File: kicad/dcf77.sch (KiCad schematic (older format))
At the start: 5 parts, among them U4 DCF77_Generic

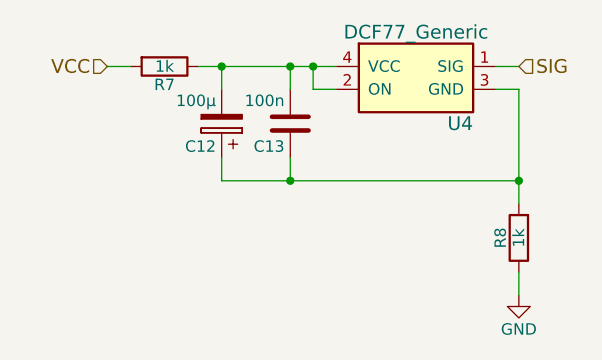
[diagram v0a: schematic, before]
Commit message: Finish schematic
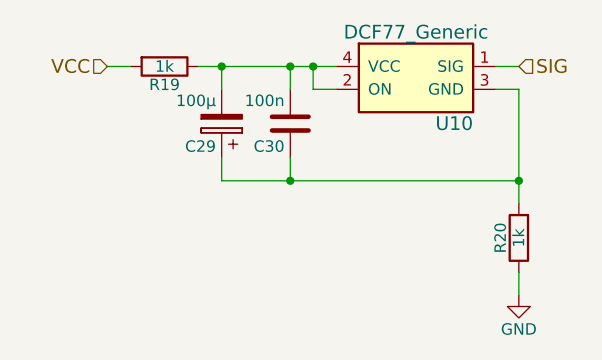
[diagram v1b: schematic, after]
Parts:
- renumbered C12 to C29, C13 to C30, R7 to R19, R8 to R20, U4 to U10
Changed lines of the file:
@@
 $Descr A4 11693 8268
 encoding utf-8
-Sheet 3 5
-Title ""
-Date ""
-Rev ""
+Sheet 5 5
+Title "E-Ink Clock"
+Date "2017-03-29"
+Rev "1.0"
 Comp ""
 Comment1 ""
@@
 $EndDescr
 $Comp
-L DCF77_Generic U4
+L DCF77_Generic U10
 U 1 1 58DE81CA
 P 2400 1050
-F 0 "U4" H 2650 850 60  0000 R CNN
+F 0 "U10" H 2650 850 60  0000 R CNN
 F 1 "DCF77_Generic" H 2400 1250 60  0000 C CNN
 F 2 "" H 2400 1200 60  0001 C CNN
@@
 $EndComp
 $Comp
-L GND #PWR020
+L GND #PWR21
 U 1 1 58DE81D1
 P 2850 2000
-F 0 "#PWR020" H 2850 1750 50  0001 C CNN
+F 0 "#PWR21" H 2850 1750 50  0001 C CNN
 F 1 "GND" H 2850 1850 50  0000 C CNN
 F 2 "" H 2850 2000 50  0000 C CNN
@@
 $EndComp
 $Comp
-L C C13
+L C C30
 U 1 1 58DE81D9
 P 1850 1250
-F 0 "C13" H 1875 1350 50  0000 L CNN
+F 0 "C30" H 1875 1350 50  0000 L CNN
 F 1 "100n" H 1875 1150 50  0000 L CNN
 F 2 "" H 1888 1100 50  0001 C CNN
@@
 $EndComp
 $Comp
-L CP C12
+L CP C29
 U 1 1 58DE81E0
 P 1550 1250
-F 0 "C12" H 1575 1350 50  0000 L CNN
+F 0 "C29" H 1575 1350 50  0000 L CNN
 F 1 "100µ" H 1575 1150 50  0000 L CNN
 F 2 "" H 1588 1100 50  0001 C CNN
@@
 $EndComp
 $Comp
-L R R7
+L R R19
 U 1 1 58DE81E9
 P 1300 1000
-F 0 "R7" V 1380 1000 50  0000 C CNN
+F 0 "R19" V 1380 1000 50  0000 C CNN
 F 1 "1k" V 1300 1000 50  0000 C CNN
 F 2 "" V 1230 1000 50  0001 C CNN
@@
 $EndComp
 $Comp
-L R R8
+L R R20
 U 1 1 58DE81F0
 P 2850 1750
-F 0 "R8" V 2930 1750 50  0000 C CNN
+F 0 "R20" V 2930 1750 50  0000 C CNN
 F 1 "1k" V 2850 1750 50  0000 C CNN
 F 2 "" V 2780 1750 50  0001 C CNN

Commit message: Set most footprints
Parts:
- C29, C30: footprint (none) -> Capacitors_SMD:C_0805_HandSoldering
- R19, R20: footprint (none) -> Resistors_SMD:R_0805_HandSoldering
- U10: footprint (none) -> einkclock:Reichelt_DCF77_Module
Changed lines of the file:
@@
 F 0 "U10" H 2650 850 60  0000 R CNN
 F 1 "DCF77_Generic" H 2400 1250 60  0000 C CNN
-F 2 "" H 2400 1200 60  0001 C CNN
+F 2 "einkclock:Reichelt_DCF77_Module" H 2400 1200 60  0001 C CNN
 F 3 "" H 2400 1200 60  0001 C CNN
 	1    2400 1050
@@
 $EndComp
 $Comp
-L GND #PWR21
+L GND #PWR021
 U 1 1 58DE81D1
 P 2850 2000
-F 0 "#PWR21" H 2850 1750 50  0001 C CNN
+F 0 "#PWR021" H 2850 1750 50  0001 C CNN
 F 1 "GND" H 2850 1850 50  0000 C CNN
 F 2 "" H 2850 2000 50  0000 C CNN
@@
 F 0 "C30" H 1875 1350 50  0000 L CNN
 F 1 "100n" H 1875 1150 50  0000 L CNN
-F 2 "" H 1888 1100 50  0001 C CNN
+F 2 "Capacitors_SMD:C_0805_HandSoldering" H 1888 1100 50  0001 C CNN
 F 3 "" H 1850 1250 50  0000 C CNN
 	1    1850 1250
@@
 F 0 "C29" H 1575 1350 50  0000 L CNN
 F 1 "100µ" H 1575 1150 50  0000 L CNN
-F 2 "" H 1588 1100 50  0001 C CNN
+F 2 "Capacitors_SMD:C_0805_HandSoldering" H 1588 1100 50  0001 C CNN
 F 3 "" H 1550 1250 50  0000 C CNN
 	1    1550 1250
@@
 F 0 "R19" V 1380 1000 50  0000 C CNN
 F 1 "1k" V 1300 1000 50  0000 C CNN
-F 2 "" V 1230 1000 50  0001 C CNN
+F 2 "Resistors_SMD:R_0805_HandSoldering" V 1230 1000 50  0001 C CNN
 F 3 "" H 1300 1000 50  0000 C CNN
 	1    1300 1000
@@
 F 0 "R20" V 2930 1750 50  0000 C CNN
 F 1 "1k" V 2850 1750 50  0000 C CNN
-F 2 "" V 2780 1750 50  0001 C CNN
+F 2 "Resistors_SMD:R_0805_HandSoldering" V 2780 1750 50  0001 C CNN
 F 3 "" H 2850 1750 50  0000 C CNN
 	1    2850 1750

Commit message: First routing
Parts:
- C29, C30: footprint Capacitors_SMD:C_0805_HandSoldering -> Resistors_SMD:R_0805_HandSoldering
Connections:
- net at C29.2, C30.2, R19.1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: no longer U10.2 (ON)
- net at C29.1, C30.1, R20.2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: now also U10.2 (ON)
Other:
- moved on the sheet: C29, C30, R19
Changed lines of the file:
@@
 L C C30
 U 1 1 58DE81D9
-P 1850 1250
-F 0 "C30" H 1875 1350 50  0000 L CNN
-F 1 "100n" H 1875 1150 50  0000 L CNN
-F 2 "Capacitors_SMD:C_0805_HandSoldering" H 1888 1100 50  0001 C CNN
-F 3 "" H 1850 1250 50  0000 C CNN
-	1    1850 1250
+P 1750 1250
+F 0 "C30" H 1775 1350 50  0000 L CNN
+F 1 "100n" H 1775 1150 50  0000 L CNN
+F 2 "Resistors_SMD:R_0805_HandSoldering" H 1788 1100 50  0001 C CNN
+F 3 "" H 1750 1250 50  0000 C CNN
+	1    1750 1250
 	-1   0    0    1
 $EndComp
@@
 L CP C29
 U 1 1 58DE81E0
-P 1550 1250
-F 0 "C29" H 1575 1350 50  0000 L CNN
-F 1 "100µ" H 1575 1150 50  0000 L CNN
-F 2 "Capacitors_SMD:C_0805_HandSoldering" H 1588 1100 50  0001 C CNN
-F 3 "" H 1550 1250 50  0000 C CNN
-	1    1550 1250
+P 1450 1250
+F 0 "C29" H 1475 1350 50  0000 L CNN
+F 1 "100µ" H 1475 1150 50  0000 L CNN
+F 2 "Resistors_SMD:R_0805_HandSoldering" H 1488 1100 50  0001 C CNN
+F 3 "" H 1450 1250 50  0000 C CNN
+	1    1450 1250
 	-1   0    0    1
 $EndComp
@@
 L R R19
 U 1 1 58DE81E9
-P 1300 1000
-F 0 "R19" V 1380 1000 50  0000 C CNN
-F 1 "1k" V 1300 1000 50  0000 C CNN
-F 2 "Resistors_SMD:R_0805_HandSoldering" V 1230 1000 50  0001 C CNN
-F 3 "" H 1300 1000 50  0000 C CNN
-	1    1300 1000
+P 1200 1000
+F 0 "R19" V 1280 1000 50  0000 C CNN
+F 1 "1k" V 1200 1000 50  0000 C CNN
+F 2 "Resistors_SMD:R_0805_HandSoldering" V 1130 1000 50  0001 C CNN
+F 3 "" H 1200 1000 50  0000 C CNN
+	1    1200 1000
 	0    1    1    0
 $EndComp
@@
 	-1   0    0    1
 $EndComp
-Text HLabel 1050 1000 0    60   Input ~ 0
+Text HLabel 950  1000 0    60   Input ~ 0
 VCC
 Text HLabel 2850 1000 2    60   Input ~ 0
@@
 	2750 1100 2850 1100
 Wire Wire Line
-	1450 1000 2050 1000
-Wire Wire Line
-	1950 1000 1950 1100
+	1350 1000 2050 1000
 Wire Wire Line
 	1950 1100 2050 1100
-Connection ~ 1950 1000
 Wire Wire Line
-	1550 1100 1550 1000
-Connection ~ 1550 1000
+	1450 1100 1450 1000
+Connection ~ 1450 1000
 Wire Wire Line
-	1850 1100 1850 1000
-Connection ~ 1850 1000
+	1750 1100 1750 1000
+Connection ~ 1750 1000
 Wire Wire Line
 	2750 1000 2850 1000
@@
 	2850 1900 2850 2000
 Wire Wire Line
-	1550 1400 1550 1500
+	1450 1400 1450 1500
 Wire Wire Line
-	1550 1500 2850 1500
-Wire Wire Line
-	1850 1400 1850 1500
-Connection ~ 1850 1500
+	1750 1400 1750 1500
+Connection ~ 1750 1500
 Wire Wire Line
 	2850 1100 2850 1600
 Connection ~ 2850 1500
 Wire Wire Line
-	1050 1000 1150 1000
+	950  1000 1050 1000
+Wire Wire Line
+	1950 1500 1950 1100
+Wire Wire Line
+	1450 1500 2850 1500
+Connection ~ 1950 1500
 $EndSCHEMATC

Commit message: Add BOM
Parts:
- removed C29: 100µ, Resistors_SMD:R_0805_HandSoldering, symbol CP
- added C29: 100µ, Resistors_SMD:R_1206_HandSoldering, symbol C
- C30: Manf# (none) -> 885012207098
- R19, R20: Manf# (none) -> ERJ-6ENF1001V
- U10: Manf# (none) -> DCF77 MODUL
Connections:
- net at C30.1, R20.2, U10.2 (ON)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: now also C29.1
- net at C30.2, R19.1, U10.4 (VCC): now also C29.2
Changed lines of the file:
@@
 F 2 "einkclock:Reichelt_DCF77_Module" H 2400 1200 60  0001 C CNN
 F 3 "" H 2400 1200 60  0001 C CNN
+F 4 "DCF77 MODUL" H 2400 1050 60  0001 C CNN "Manf#"
 	1    2400 1050
 	1    0    0    -1
@@
 F 2 "Resistors_SMD:R_0805_HandSoldering" H 1788 1100 50  0001 C CNN
 F 3 "" H 1750 1250 50  0000 C CNN
+F 4 "885012207098" H 1750 1250 60  0001 C CNN "Manf#"
 	1    1750 1250
-	-1   0    0    1
-$EndComp
-$Comp
-L CP C29
-U 1 1 58DE81E0
-P 1450 1250
-F 0 "C29" H 1475 1350 50  0000 L CNN
-F 1 "100µ" H 1475 1150 50  0000 L CNN
-F 2 "Resistors_SMD:R_0805_HandSoldering" H 1488 1100 50  0001 C CNN
-F 3 "" H 1450 1250 50  0000 C CNN
-	1    1450 1250
 	-1   0    0    1
 $EndComp
@@
 F 2 "Resistors_SMD:R_0805_HandSoldering" V 1130 1000 50  0001 C CNN
 F 3 "" H 1200 1000 50  0000 C CNN
+F 4 "ERJ-6ENF1001V" V 1200 1000 60  0001 C CNN "Manf#"
 	1    1200 1000
 	0    1    1    0
@@
 F 2 "Resistors_SMD:R_0805_HandSoldering" V 2780 1750 50  0001 C CNN
 F 3 "" H 2850 1750 50  0000 C CNN
+F 4 "ERJ-6ENF1001V" V 2850 1750 60  0001 C CNN "Manf#"
 	1    2850 1750
 	-1   0    0    1
@@
 	1450 1500 2850 1500
 Connection ~ 1950 1500
+$Comp
+L C C29
+U 1 1 58E46F0E
+P 1450 1250
+F 0 "C29" H 1475 1350 50  0000 L CNN
+F 1 "100µ" H 1475 1150 50  0000 L CNN
+F 2 "Resistors_SMD:R_1206_HandSoldering" H 1488 1100 50  0001 C CNN
+F 3 "" H 1450 1250 50  0000 C CNN
+F 4 "GRM31CD80J107ME39K" H 1450 1250 60  0001 C CNN "Manf#"
+	1    1450 1250
+	-1   0    0    1
+$EndComp
 $EndSCHEMATC
